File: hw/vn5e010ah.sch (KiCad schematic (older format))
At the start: 4 parts, among them U1001 VN5E010AH

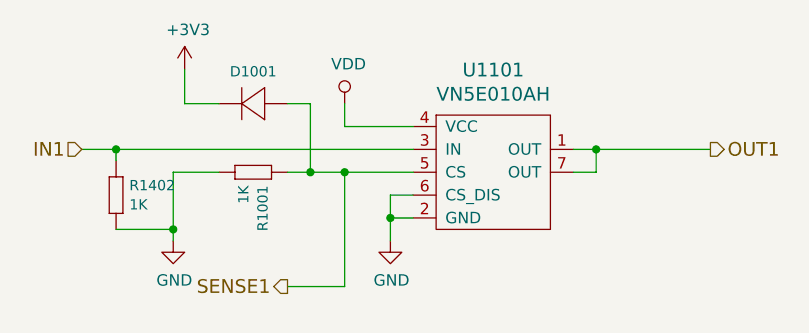
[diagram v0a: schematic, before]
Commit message: pulldown resistors added to power outputs
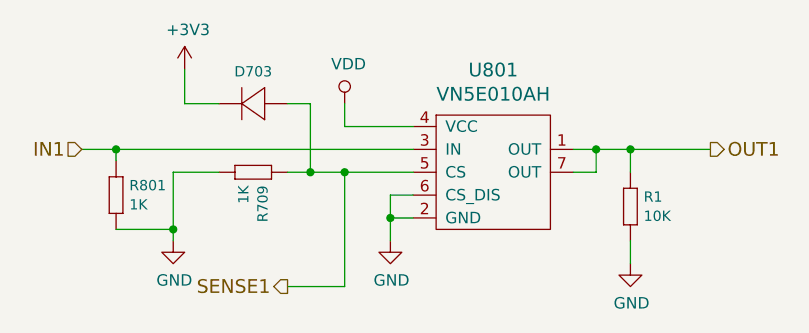
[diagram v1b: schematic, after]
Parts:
- added R1: 10K, yageo:0603, symbol yageo:10K
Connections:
- net GND: now also R1.1 (R1)
- net OUT1: now also R1.2 (R2)
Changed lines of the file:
@@
 AR Path="/5A13680F/59D7E637" Ref="#PWR048"  Part="1"
 AR Path="/5A14370A/59D7E637" Ref="#PWR051"  Part="1"
-F 0 "#PWR045" H 4600 2850 50  0001 C CNN
+F 0 "#PWR036" H 4600 2850 50  0001 C CNN
 F 1 "VDD" H 4617 3173 50  0000 C CNN
 F 2 "" H 4600 3000 50  0000 C CNN
@@
 AR Path="/5A13680F/5A014ACD" Ref="#PWR049"  Part="1"
 AR Path="/5A14370A/5A014ACD" Ref="#PWR052"  Part="1"
-F 0 "#PWR046" H 3850 3350 50  0001 C CNN
+F 0 "#PWR037" H 3850 3350 50  0001 C CNN
 F 1 "GND" H 3855 3427 50  0000 C CNN
 F 2 "" H 3850 3600 50  0000 C CNN
@@
 AR Path="/5A13680F/5A058D94" Ref="R1502"  Part="1"
 AR Path="/5A14370A/5A058D94" Ref="R1602"  Part="1"
-F 0 "R1402" V 3608 3408 45  0000 L CNN
+F 0 "R801" V 3608 3408 45  0000 L CNN
 F 1 "1K" V 3692 3408 45  0000 L CNN
 F 2 "yageo:0603" H 3630 3500 20  0001 C CNN
@@
 AR Path="/5A1358B0/5A32CF4A" Ref="U1101"  Part="1"
 AR Path="/5A13680F/5A32CF4A" Ref="U1201"  Part="1"
-F 0 "U1101" H 5250 3747 60  0000 C CNN
+F 0 "U801" H 5250 3747 60  0000 C CNN
 F 1 "VN5E010AH" H 5250 3641 60  0000 C CNN
 F 2 "usevolt:HPAK" H 4950 4250 60  0001 C CNN
@@
 AR Path="/5A1358B0/5A32CF90" Ref="#PWR047"  Part="1"
 AR Path="/5A13680F/5A32CF90" Ref="#PWR050"  Part="1"
-F 0 "#PWR047" H 4800 3350 50  0001 C CNN
+F 0 "#PWR038" H 4800 3350 50  0001 C CNN
 F 1 "GND" H 4805 3427 50  0000 C CNN
 F 2 "" H 4800 3600 50  0000 C CNN
@@
 Connection ~ 4800 3500
 Wire Wire Line
-	5700 3200 6200 3200
+	5700 3200 5850 3200
 Wire Wire Line
 	4600 3300 4900 3300
@@
 AR Path="/5A13680F/5B23824A" Ref="R1101"  Part="1"
 AR Path="/5A14370A/5B23824A" Ref="R1202"  Part="1"
-F 0 "R1001" V 4258 3358 45  0000 L CNN
+F 0 "R709" V 4258 3358 45  0000 L CNN
 F 1 "1K" V 4342 3358 45  0000 L CNN
 F 2 "yageo:0603" H 4280 3450 20  0001 C CNN
@@
 AR Path="/5A1358B0/5B23844A" Ref="D1001"  Part="1"
 AR Path="/5A13680F/5B23844A" Ref="D1101"  Part="1"
-F 0 "D1001" H 4100 2860 45  0000 C CNN
+F 0 "D703" H 4100 2860 45  0000 C CNN
 F 1 "DIODE_RS07J-GS18" H 4170 2940 45  0001 L BNN
 F 2 "usevolt:DO219AB" H 4180 3150 20  0001 C CNN
@@
 AR Path="/5A1358B0/5B23856B" Ref="#PWR0105"  Part="1"
 AR Path="/5A13680F/5B23856B" Ref="#PWR0106"  Part="1"
-F 0 "#PWR0105" H 3900 2700 50  0001 C CNN
+F 0 "#PWR0102" H 3900 2700 50  0001 C CNN
 F 1 "+3V3" H 3915 3023 50  0000 C CNN
 F 2 "" H 3900 2850 50  0000 C CNN
@@
 Wire Wire Line
 	4450 3300 4600 3300
+$Comp
+L yageo:10K R1
+U 1 1 5BA9BFAA
+P 5850 3400
+AR Path="/5A12FF64/5BA9BFAA" Ref="R1"  Part="1"
+AR Path="/5A130D3E/5BA9BFAA" Ref="R2"  Part="1"
+AR Path="/5A1349CF/5BA9BFAA" Ref="R3"  Part="1"
+AR Path="/5A1358B0/5BA9BFAA" Ref="R4"  Part="1"
+F 0 "R1" V 5858 3458 45  0000 L CNN
+F 1 "10K" V 5942 3458 45  0000 L CNN
+F 2 "yageo:0603" H 5880 3550 20  0001 C CNN
+F 3 "" H 5819 3439 60  0001 C CNN
+F 4 "" H 6219 3839 60  0001 C CNN "1st Source Part Number"
+F 5 "Digikey" H 6119 3739 60  0001 C CNN "1st Source"
+F 6 "RC0603FR-0710KL" H 6019 3639 60  0001 C CNN "Manufacturer Part Number"
+F 7 "YAGEO" H 5919 3539 60  0001 C CNN "Manufacturer"
+	1    5850 3400
+	0    1    1    0
+$EndComp
+Wire Wire Line
+	5850 3300 5850 3200
+Connection ~ 5850 3200
+Wire Wire Line
+	5850 3200 6200 3200
+$Comp
+L power:GND #PWR0106
+U 1 1 5BA9C33E
+P 5850 3700
+AR Path="/5A12FF64/5BA9C33E" Ref="#PWR0106"  Part="1"
+AR Path="/5A130D3E/5BA9C33E" Ref="#PWR0107"  Part="1"
+AR Path="/5A1349CF/5BA9C33E" Ref="#PWR0108"  Part="1"
+AR Path="/5A1358B0/5BA9C33E" Ref="#PWR0109"  Part="1"
+F 0 "#PWR0106" H 5850 3450 50  0001 C CNN
+F 1 "GND" H 5855 3527 50  0000 C CNN
+F 2 "" H 5850 3700 50  0000 C CNN
+F 3 "" H 5850 3700 50  0000 C CNN
+	1    5850 3700
+	1    0    0    -1
+$EndComp
+Wire Wire Line
+	5850 3700 5850 3600
 $EndSCHEMATC
